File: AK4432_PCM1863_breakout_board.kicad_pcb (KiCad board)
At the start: 2 copper layers, 67.7 x 49.5 mm, 64 parts, among them J1 Conn_01x02_Pin, J2 Conn_01x04_Pin, J3 Conn_01x04_Pin, J4 Conn_01x08_Pin, J5 Conn_01x07_Pin, J6 Conn_01x01_Pin, J7 Conn_01x02_Pin, J8 Conn_01x02_Pin, U1 LD1117S33TR_SOT223, U2 LD1117S33TR_SOT223, U3 PCM1863DBTR, U4 AK4432VT, U5 SN74HC74DR, U6 SN74LVC1G04DCKR, Y1 ECS-3225MV-491.52

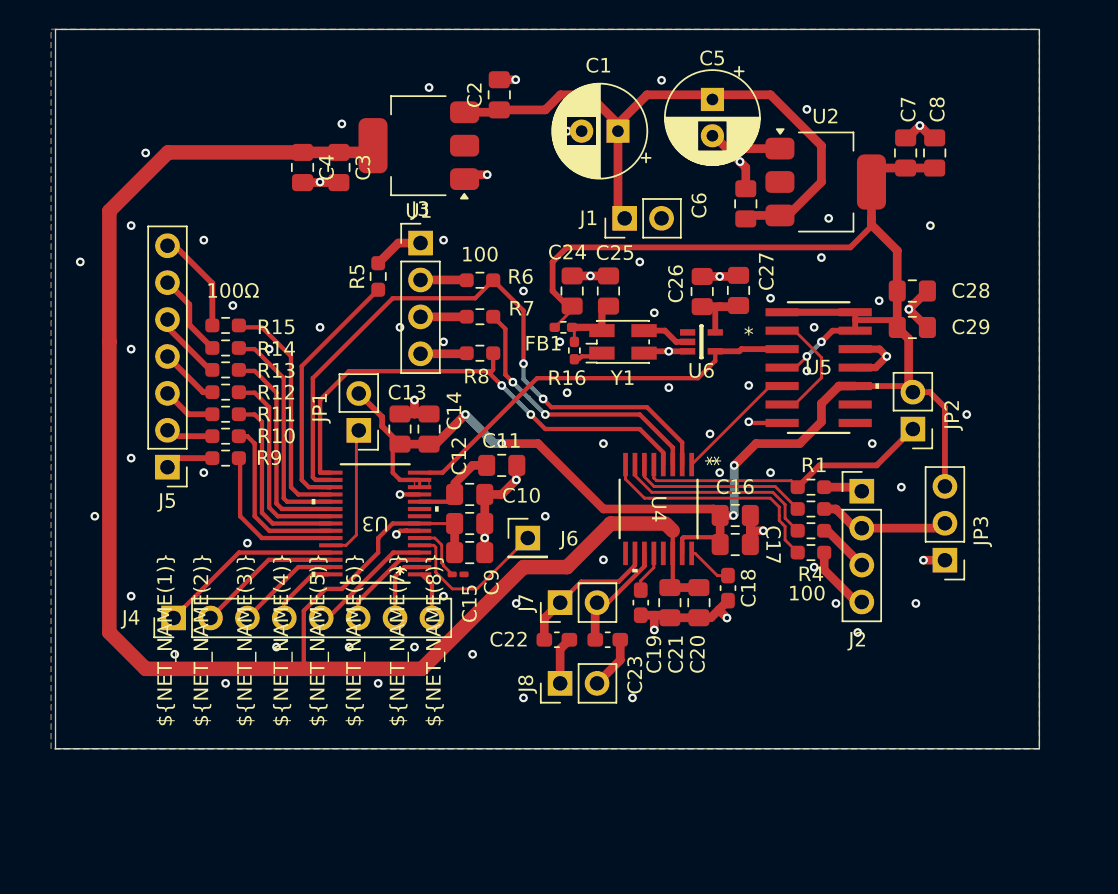
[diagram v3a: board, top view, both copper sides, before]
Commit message: Finished v1 layout! Also swaped flip-flop chip for a faster one.
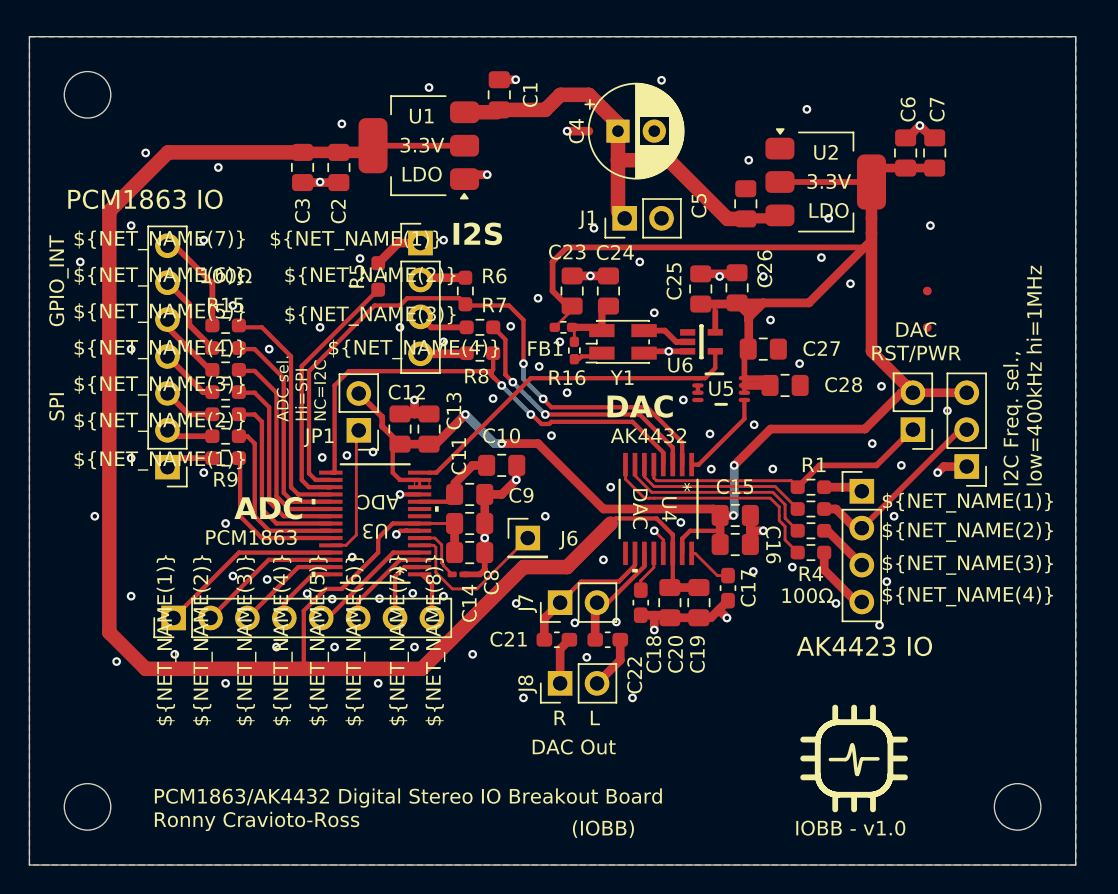
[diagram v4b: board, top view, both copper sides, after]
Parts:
- removed the C1 at (105.0, 46.0)
- added H1: MountingHole, MountingHole:MountingHole_3.2mm_M3, F.Cu at (68.5, 43.5)
- added H2: MountingHole, MountingHole:MountingHole_3.2mm_M3, F.Cu at (68.5, 92.5)
- added H3: MountingHole, MountingHole:MountingHole_3.2mm_M3, F.Cu at (132.5, 92.5)
- U5: value SN74HC74DR -> SN74LVC1G74DCUR; footprint footprints:D14-M -> footprints:DCU0008A_N
- moved C27 11.0 mm to (115.0, 61.0)
- moved C28 9.62 mm to (116.5, 63.5)
- moved U5 6.87 mm to (112.1, 63.8)
- moved C4 6.86 mm to (105.0, 46.0), turned to 0 degrees
- moved JP3 6.62 mm to (129.0, 69.1)
- moved R6 1.24 mm to (94.5, 57.0), turned to 90 degrees
- moved R7 0.73 mm to (95.5, 59.5)
- moved C25 0.21 mm to (110.7, 56.9)
- moved C26 0.21 mm to (113.2, 56.8)
- renumbered C2 to C1, C11 to C10, C12 to C11, C13 to C12, C14 to C13, C15 to C14, C16 to C15, C17 to C16, C18 to C17, C19 to C18, C20 to C19, C3 to C2, C21 to C20, C22 to C21, C23 to C22, C24 to C23, C25 to C24, C26 to C25, C27 to C26, C28 to C27, C29 to C28, C4 to C3, C5 to C4, C6 to C5, C7 to C6, C8 to C7, C9 to C8, C10 to C9
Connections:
- net /AK_CS/I2CFIL renamed /AK_CS_I2CFIL
- net /AK_CS/I2CFIL_R renamed /CS_I2CFreq
- net /AK_PDN/RST renamed /AK_PD_RST
- net /AK_SCL/CCLK renamed /AK_SCL_CCLK
- net /AK_SDA/CDTI renamed /AK_SDA_CDTI
- net /GPIO1/INTA renamed /GPIO1_INTA
- net /GPIO2/INTB renamed /GPIO2_INTB
- net /GPIO3/INTC renamed /GPIO3_INTC
- net Net-(J2-Pin_1) renamed /PWR_RST
- net Net-(J2-Pin_3) renamed /SCL_CCLK
- net Net-(J2-Pin_4) renamed /SDA_CDTI
- net Net-(J3-Pin_1) renamed /DOUT_ADC
- net Net-(J3-Pin_2) renamed /BCK
- net Net-(J3-Pin_3) renamed /DIN_DAC
- net Net-(J3-Pin_4) renamed /LRCK
- net Net-(J5-Pin_1) renamed /CS
- net Net-(J5-Pin_2) renamed /SCLK
- net Net-(J5-Pin_3) renamed /MOSI
- net Net-(J5-Pin_4) renamed /MISO
- net Net-(J5-Pin_5) renamed /1_A
- net Net-(J5-Pin_6) renamed /2_B
- net Net-(J5-Pin_7) renamed /3_C
- net Net-(J7-Pin_1) renamed /DAC_OUTR
- net Net-(J7-Pin_2) renamed /DAC_OUTL
- U5 pad 1: /+3.3_digital -> /SCKI
- U5 pad 2: Net-(U5-*1Q) -> Net-(U5-D)
- U5 pad 3: /SCKI -> Net-(U5-D)
- U5 pad 4: /+3.3_digital -> GND
- U5 pad 6: Net-(U5-*1Q) -> /+3.3_digital
- U5 pad 7: GND -> /+3.3_digital
- U5 pad 8: unconnected-(U5-*2Q-Pad8) -> /+3.3_digital
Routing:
- net GND: track 64.6 -> 48.6 mm, vias 79 -> 102
- net +5V: track 43.6 -> 32.0 mm
- net /+3.3_digital: track 137.3 -> 148.6 mm, vias 6 -> 4
- net Net-(U5-*1Q): track 8.33 -> 0.00 mm
- net /+3.3_analog: track 119.3 -> 125.1 mm
- net /SCKI: track 29.1 -> 24.5 mm
- net /CS_I2CFreq: track 9.43 -> 13.6 mm
- net /MCLK_AKM: track 8.46 -> 6.23 mm
- net /I2S_BCK: track 45.3 -> 44.5 mm
- net /I2S_DIN_DAC: track 19.1 -> 18.4 mm
- net Net-(U5-D): track 0.00 -> 0.50 mm
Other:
- board size 67.7 x 49.5 mm -> 72 x 57 mm
- board text added: "(IOBB)"
- board text added: "3.3V"
- board text added: "ADC"
- board text added: "ADC sel. Hi=SPI NC=I2C"
- board text added: "AK4423 IO"
- board text added: "AK4432"
- board text added: "DAC"
- board text added: "DAC Out"
- board text added: "DAC RST/PWR"
- board text added: "GPIO_INT"
- board text added: "I2C Freq. sel., low=400kHz hi=1MHz"
- board text added: "I2S"
- board text added: "IOBB - v1.0"
- board text added: "L"
- board text added: "LDO"
- board text added: "PCM1863"
- board text added: "PCM1863 IO"
- board text added: "PCM1863/AK4432 Digital Stereo IO Breakout Board Ronny Cravioto-Ross"
- board text added: "R"
- board text added: "SPI"

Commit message: Made final v1 changes and ordered from JLC!
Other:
- board text added: "248nonny.github.io"
- board text added: "github.com/248nonny/Digital_Stereo_IO_Breakout_Board"
